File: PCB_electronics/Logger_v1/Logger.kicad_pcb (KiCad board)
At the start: 2 copper layers, 90 x 57.5 mm, 27 parts, among them P1 GPS_breakout_connector, P10 CONN_01X03, P11 CONN_01X02, P12 CONN_01X02, P13 CONN_01X02, P14 CONN_01X02, P15 CONN_01X02, P2 SD_breakout_connector, P3 Iridium_connector, P4 VN100_connector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

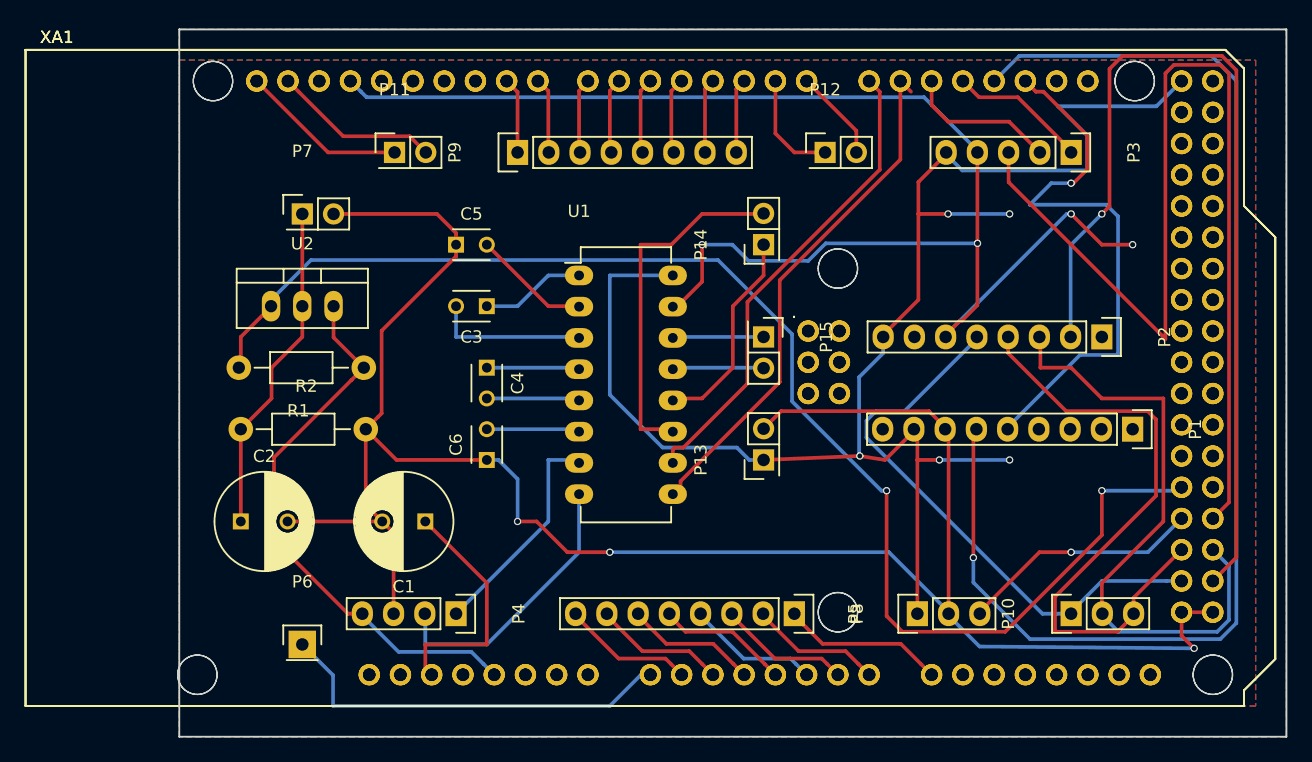
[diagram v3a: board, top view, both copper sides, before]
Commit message: ordered first prototype logger shield
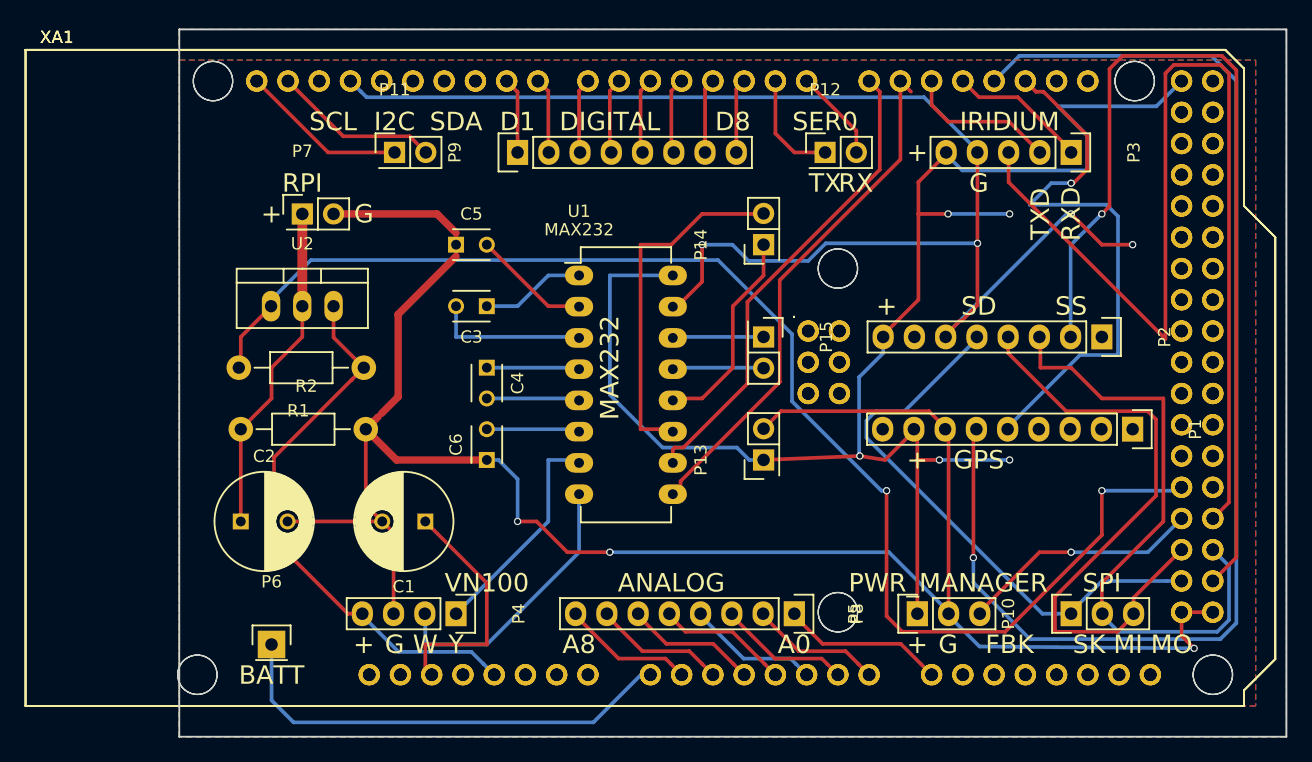
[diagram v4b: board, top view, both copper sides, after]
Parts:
- moved P6 2.50 mm to (132.5, 135.0)
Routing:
- net /BATT_+: track 32.9 -> 37.7 mm
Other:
- board text added: "+"
- board text added: "A0"
- board text added: "A8"
- board text added: "ANALOG"
- board text added: "BATT"
- board text added: "D1"
- board text added: "D8"
- board text added: "DIGITAL"
- board text added: "FBK"
- board text added: "G"
- board text added: "GPS"
- board text added: "I2C"
- board text added: "IRIDIUM"
- board text added: "Logger v 1.0 Jean Rabault, UiO 05-2018"
- board text added: "MAX232"
- board text added: "PWR_MANAGER"
- board text added: "RPI"
- board text added: "RX"
- board text added: "RXD"
- board text added: "SCL"
- board text added: "SD"
- board text added: "SDA"
- board text added: "SER0"
- board text added: "SK MI MO"
- board text added: "SPI"
- board text added: "SS"
- board text added: "TX"
- board text added: "TXD"
- board text added: "VN100"
- board text added: "W"
- board text added: "Y"
